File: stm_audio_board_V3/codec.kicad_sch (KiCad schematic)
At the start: 8 parts

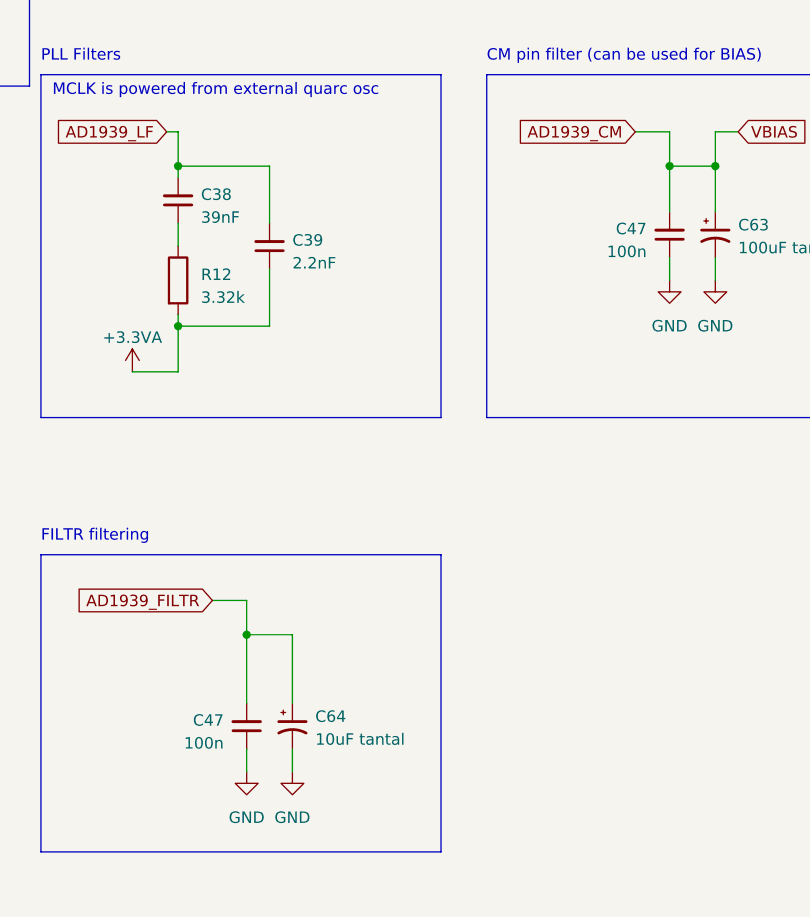
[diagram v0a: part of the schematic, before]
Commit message: minor changes to components
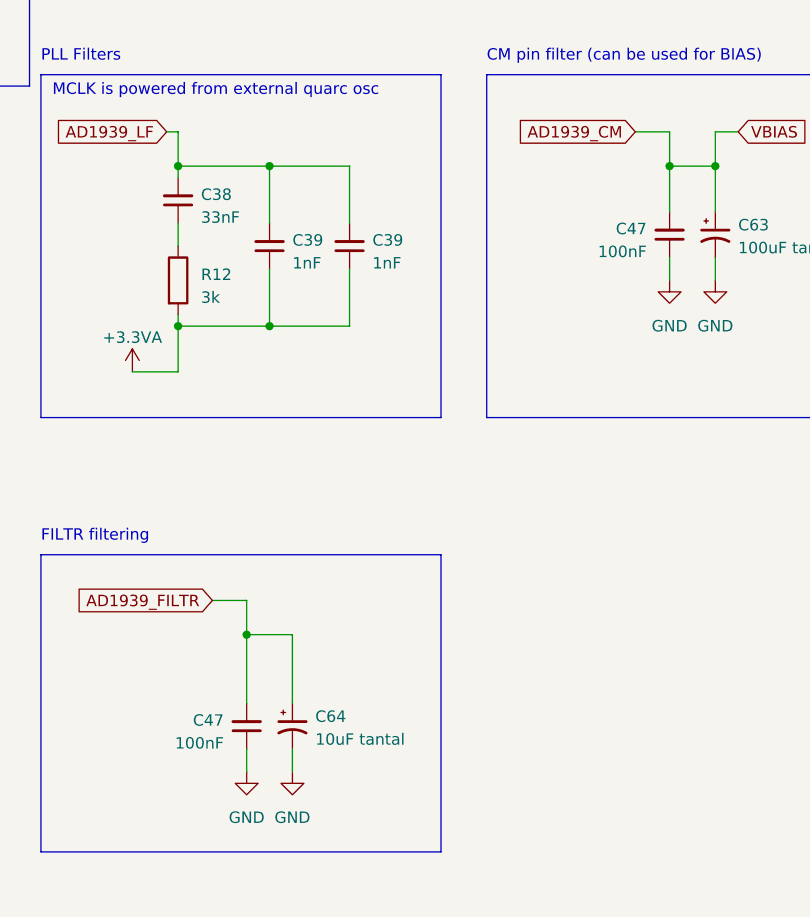
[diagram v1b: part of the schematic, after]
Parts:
- added C39: 1nF, Capacitor_SMD:C_0603_1608Metric, symbol Device:C_Small
- C38: value 39nF -> 33nF; JLCPCB (none) -> C21117; LCSC Part (none) -> C21117
- C39: value 2.2nF -> 1nF; JLCPCB (none) -> C1588; LCSC Part (none) -> C1588
- C47: value 100n -> 100nF; JLCPCB (none) -> C14663; LCSC Part (none) -> C14663
- C63: LCSC Part (none) -> C16133
- C64: LCSC Part (none) -> C7171
- R12: value 3.32k -> 3k; JLCPCB (none) -> C4211; LCSC Part (none) -> C4211
- U11: LCSC Part (none) -> C2913556
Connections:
- net +3.3VA: now also C39.1
- net AD1939_LF: now also C39.2
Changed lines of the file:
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@@
   (junction (at 152.4 58.42) (diameter 0) (color 0 0 0 0)
+  )
+  (junction (at 162.56 40.64) (diameter 0) (color 0 0 0 0)
+  )
+  (junction (at 162.56 58.42) (diameter 0) (color 0 0 0 0)
   )
   (junction (at 207.01 40.64) (diameter 0) (color 0 0 0 0)
@@
     (stroke (width 0) (type default))
   )
+  (wire (pts (xy 171.45 46.99) (xy 171.45 40.64))
+    (stroke (width 0) (type default))
+  )
   (wire (pts (xy 152.4 46.99) (xy 152.4 49.53))
     (stroke (width 0) (type default))
@@
     (stroke (width 0) (type default))
   )
+  (wire (pts (xy 162.56 52.07) (xy 162.56 58.42))
+    (stroke (width 0) (type default))
+  )
   (wire (pts (xy 152.4 57.15) (xy 152.4 58.42))
     (stroke (width 0) (type default))
@@
     (stroke (width 0) (type default))
   )
+  (wire (pts (xy 171.45 40.64) (xy 162.56 40.64))
+    (stroke (width 0) (type default))
+  )
   (wire (pts (xy 34.29 109.22) (xy 44.45 109.22))
     (stroke (width 0) (type default))
@@
     (stroke (width 0) (type default))
   )
+  (wire (pts (xy 162.56 58.42) (xy 171.45 58.42))
+    (stroke (width 0) (type default))
+  )
   (wire (pts (xy 39.37 40.64) (xy 44.45 40.64))
     (stroke (width 0) (type default))
   )
-  (wire (pts (xy 162.56 58.42) (xy 162.56 52.07))
-    (stroke (width 0) (type default))
-  )
   (wire (pts (xy 165.1 92.71) (xy 165.1 100.33))
     (stroke (width 0) (type default))
@@
     (stroke (width 0) (type default))
   )
+  (wire (pts (xy 171.45 52.07) (xy 171.45 58.42))
+    (stroke (width 0) (type default))
+  )
+  (wire (pts (xy 39.37 45.72) (xy 44.45 45.72))
+    (stroke (width 0) (type default))
+  )
+  (wire (pts (xy 41.91 88.9) (xy 44.45 88.9))
+    (stroke (width 0) (type default))
+  )
+  (wire (pts (xy 152.4 40.64) (xy 162.56 40.64))
+    (stroke (width 0) (type default))
+  )
+  (wire (pts (xy 34.29 111.76) (xy 44.45 111.76))
+    (stroke (width 0) (type default))
+  )
   (wire (pts (xy 162.56 40.64) (xy 162.56 46.99))
-    (stroke (width 0) (type default))
-  )
-  (wire (pts (xy 39.37 45.72) (xy 44.45 45.72))
-    (stroke (width 0) (type default))
-  )
-  (wire (pts (xy 41.91 88.9) (xy 44.45 88.9))
-    (stroke (width 0) (type default))
-  )
-  (wire (pts (xy 152.4 40.64) (xy 162.56 40.64))
-    (stroke (width 0) (type default))
-  )
-  (wire (pts (xy 34.29 111.76) (xy 44.45 111.76))
     (stroke (width 0) (type default))
   )
@@
     )
     (property "JLCPCB" "C2913556" (at 60.96 27.94 0)
+      (effects (font (size 1.27 1.27)) hide)
+    )
+    (property "LCSC Part" "C2913556" (at 60.96 27.94 0)
       (effects (font (size 1.27 1.27)) hide)
     )
@@
       (effects (font (size 1.27 1.27)) (justify left))
     )
-    (property "Value" "3.32k" (at 154.94 55.245 0)
+    (property "Value" "3k" (at 154.94 55.245 0)
       (effects (font (size 1.27 1.27)) (justify left))
     )
@@
     )
     (property "Datasheet" "~" (at 152.4 53.34 0)
+      (effects (font (size 1.27 1.27)) hide)
+    )
+    (property "JLCPCB" "C4211" (at 152.4 53.34 0)
+      (effects (font (size 1.27 1.27)) hide)
+    )
+    (property "LCSC Part" "C4211" (at 152.4 53.34 0)
       (effects (font (size 1.27 1.27)) hide)
     )
@@
       (effects (font (size 1.27 1.27)) hide)
     )
+    (property "LCSC Part" "C7171" (at 165.1 102.87 0)
+      (effects (font (size 1.27 1.27)) hide)
+    )
     (pin "1")
     (pin "2")
@@
       (effects (font (size 1.27 1.27)) (justify right))
     )
-    (property "Value" "39nF" (at 154.94 46.3486 0)
+    (property "Value" "33nF" (at 154.94 46.3486 0)
       (effects (font (size 1.27 1.27)) (justify right))
     )
@@
     )
     (property "Datasheet" "~" (at 152.4 44.45 0)
+      (effects (font (size 1.27 1.27)) hide)
+    )
+    (property "JLCPCB" "C21117" (at 152.4 44.45 0)
+      (effects (font (size 1.27 1.27)) hide)
+    )
+    (property "LCSC Part" "C21117" (at 152.4 44.45 0)
       (effects (font (size 1.27 1.27)) hide)
     )
@@
       (effects (font (size 1.27 1.27)) (justify right))
     )
-    (property "Value" "100n" (at 204.47 50.1586 0)
+    (property "Value" "100nF" (at 204.47 50.1586 0)
       (effects (font (size 1.27 1.27)) (justify right))
     )
@@
     )
     (property "Datasheet" "~" (at 207.01 48.26 0)
+      (effects (font (size 1.27 1.27)) hide)
+    )
+    (property "JLCPCB" "C14663" (at 207.01 48.26 0)
+      (effects (font (size 1.27 1.27)) hide)
+    )
+    (property "LCSC Part" "C14663" (at 207.01 48.26 0)
       (effects (font (size 1.27 1.27)) hide)
     )
@@
     )
   )
+  (symbol (lib_id "Device:C_Small") (at 171.45 49.53 180) (unit 1)
+    (in_bom yes) (on_board yes) (dnp no) (fields_autoplaced)
+    (property "Reference" "C39" (at 173.99 48.8886 0)
+      (effects (font (size 1.27 1.27)) (justify right))
+    )
+    (property "Value" "1nF" (at 173.99 51.4286 0)
+      (effects (font (size 1.27 1.27)) (justify right))
+    )
+    (property "Footprint" "Capacitor_SMD:C_0603_1608Metric" (at 171.45 49.53 0)
+      (effects (font (size 1.27 1.27)) hide)
+    )
+    (property "Datasheet" "~" (at 171.45 49.53 0)
+      (effects (font (size 1.27 1.27)) hide)
+    )
+    (property "JLCPCB" "C1588" (at 171.45 49.53 0)
+      (effects (font (size 1.27 1.27)) hide)
+    )
+    (property "LCSC Part" "C1588" (at 171.45 49.53 0)
+      (effects (font (size 1.27 1.27)) hide)
+    )
+    (pin "1")
+    (pin "2")
+    (instances
+      (project "stm_audio_board_V3"
+        (path "/6997cf63-2615-4e49-9471-e7da1b6bae71"
+          (reference "C39") (unit 1)
+        )
+        (path "/6997cf63-2615-4e49-9471-e7da1b6bae71/927539c8-c0d0-4950-9b67-385a1cdd80f8"
+          (reference "C39") (unit 1)
+        )
+        (path "/6997cf63-2615-4e49-9471-e7da1b6bae71/83920463-7bb1-4088-aad8-702bcdea14ea"
+          (reference "C39") (unit 1)
+        )
+        (path "/6997cf63-2615-4e49-9471-e7da1b6bae71/8744407a-1e34-4228-b7c6-9fdc39f322d4"
+          (reference "C228") (unit 1)
+        )
+      )
+    )
+  )
   (symbol (lib_id "power:+3.3V") (at 35.56 101.6 0) (unit 1)
     (in_bom yes) (on_board yes) (dnp no) (fields_autoplaced)
@@
       (effects (font (size 1.27 1.27)) (justify right))
     )
-    (property "Value" "2.2nF" (at 165.1 51.4286 0)
+    (property "Value" "1nF" (at 165.1 51.4286 0)
       (effects (font (size 1.27 1.27)) (justify right))
     )
@@
     )
     (property "Datasheet" "~" (at 162.56 49.53 0)
+      (effects (font (size 1.27 1.27)) hide)
+    )
+    (property "JLCPCB" "C1588" (at 162.56 49.53 0)
+      (effects (font (size 1.27 1.27)) hide)
+    )
+    (property "LCSC Part" "C1588" (at 162.56 49.53 0)
       (effects (font (size 1.27 1.27)) hide)
     )
@@
       (effects (font (size 1.27 1.27)) hide)
     )
+    (property "LCSC Part" "C16133" (at 212.09 48.26 0)
+      (effects (font (size 1.27 1.27)) hide)
+    )
     (pin "1")
     (pin "2")
@@
       (effects (font (size 1.27 1.27)) (justify right))
     )
-    (property "Value" "100n" (at 157.48 104.7686 0)
+    (property "Value" "100nF" (at 157.48 104.7686 0)
       (effects (font (size 1.27 1.27)) (justify right))
     )
@@
       (effects (font (size 1.27 1.27)) hide)
     )
+    (property "JLCPCB" "C14663" (at 160.02 102.87 0)
+      (effects (font (size 1.27 1.27)) hide)
+    )
+    (property "LCSC Part" "C14663" (at 160.02 102.87 0)
+      (effects (font (size 1.27 1.27)) hide)
+    )
